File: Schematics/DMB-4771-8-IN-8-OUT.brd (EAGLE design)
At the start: 50 x 86.9 mm, 43 parts

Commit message: Modifications et ajout des cartes C
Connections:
- net S$47 renamed INT1
- net S$48 renamed SCL
- net S$49 renamed SDA
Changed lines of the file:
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@@
 <wire x1="25.4" y1="42.6275" x2="25.4" y2="36.9697" width="0.4064" layer="1"/>
 </signal>
-<signal name="S$48">
+<signal name="SCL">
 <contactref element="E$17" pad="12"/>
 <contactref element="E$60" pad="6"/>
@@
 <via x="14.2875" y="39.6875" extent="1-16" drill="0.5"/>
 </signal>
-<signal name="S$49">
+<signal name="SDA">
 <contactref element="E$60" pad="5"/>
 <contactref element="E$17" pad="13"/>
@@
 <wire x1="34.6075" y1="59.055" x2="34.6075" y2="62.3316" width="0.4064" layer="1"/>
 </signal>
-<signal name="S$47">
+<signal name="INT1">
 <contactref element="E$17" pad="20"/>
 <contactref element="E$60" pad="1"/>

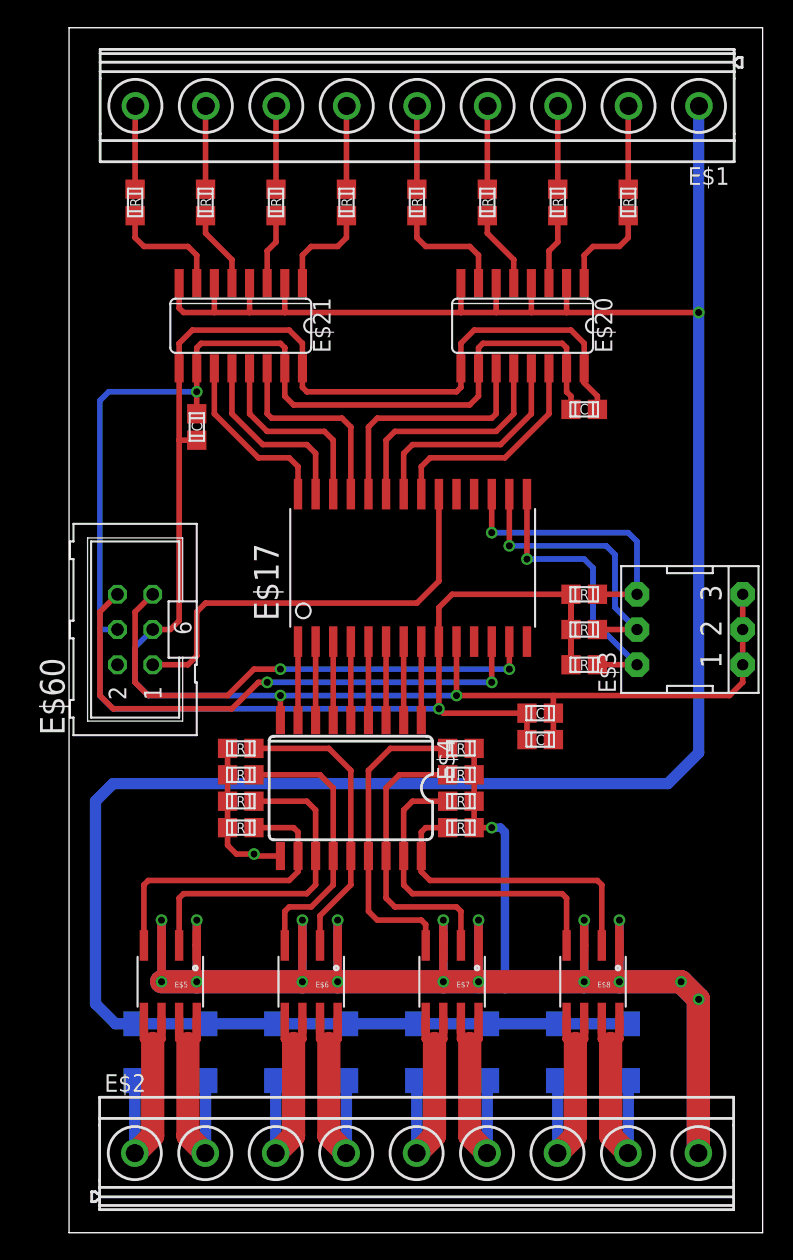
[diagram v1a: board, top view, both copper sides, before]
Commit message: Ajout cape et modification cartes C
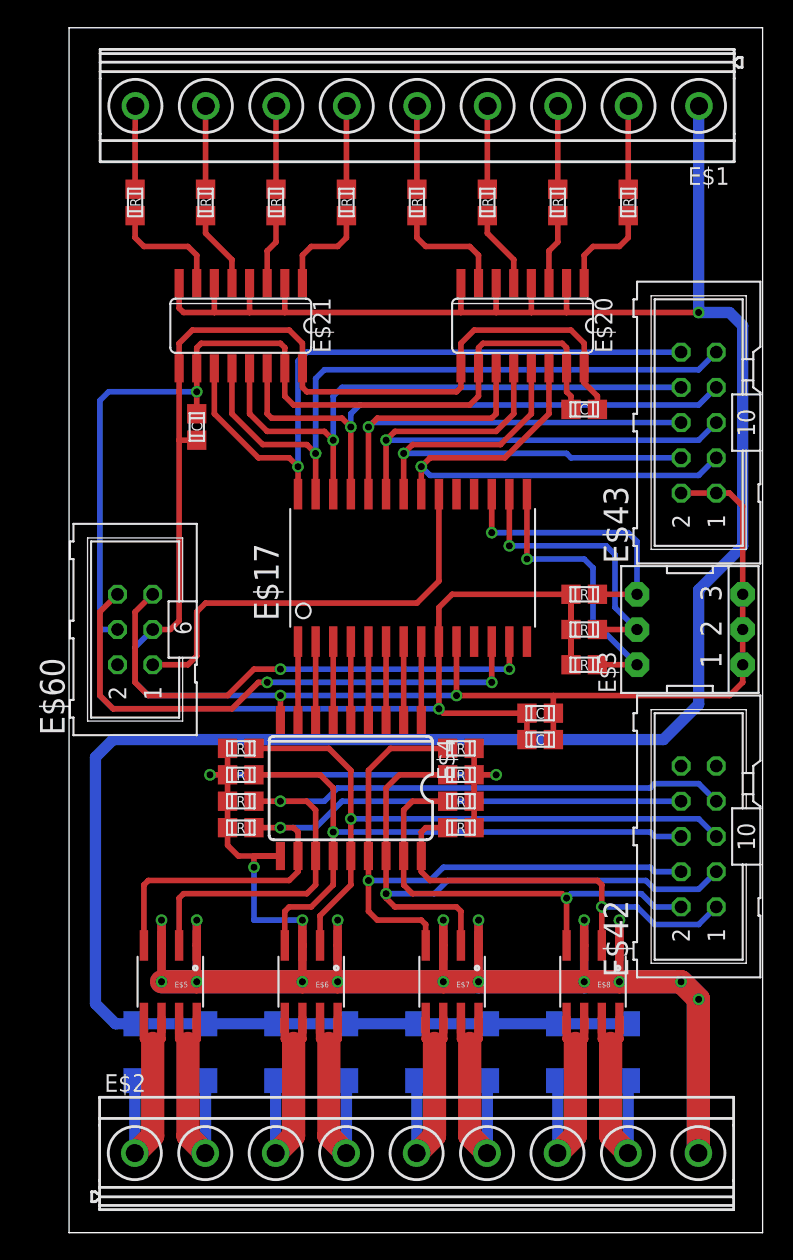
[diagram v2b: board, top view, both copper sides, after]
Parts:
- added E$42, E$43: (no value), con-harting-ml:ML10
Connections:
- removed net S$88: E$12.2, E$13.2, E$14.2, E$15.2, E$2.9, E$5.1, E$5.3, E$6.1, E$6.3, E$7.1, E$7.3, E$8.1, E$8.3
- removed net S$89: E$17.28, E$21.11
- new net S$15: E$17.28, E$21.11, E$43.10
- net GND: now also E$43.1, E$43.2
- net S$20: now also E$42.8
- net S$21: now also E$42.7
- net S$23: now also E$42.6
- net S$25: now also E$42.5
- net S$28: now also E$42.4
- net S$29: now also E$42.3
- net S$31: now also E$42.2
- net S$32: now also E$42.1
- net S$9: now also E$12.2, E$13.2, E$14.2, E$15.2, E$2.9, E$5.1, E$5.3, E$6.1, E$6.3, E$7.1, E$7.3, E$8.1, E$8.3
- net S$90: now also E$43.9
- net S$91: now also E$43.8
- net S$92: now also E$43.7
- net S$93: now also E$43.6
- net S$94: now also E$43.5
- net S$95: now also E$43.4
- net S$96: now also E$43.3
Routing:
- net S$9: track 11.1 -> 222.4 mm, vias 1 -> 20
- net S$88: track 190.9 -> 0.00 mm, vias 18 -> 0
- net S$15: track 0.00 -> 48.4 mm, vias 0 -> 1
- net S$90: track 13.4 -> 48.5 mm, vias 0 -> 1
- net S$21: track 23.8 -> 56.2 mm, vias 0 -> 1
- net S$20: track 22.0 -> 51.7 mm, vias 0 -> 1
- net S$91: track 14.0 -> 42.5 mm, vias 0 -> 1
- net S$92: track 14.5 -> 42.6 mm, vias 0 -> 1
- net S$25: track 21.2 -> 48.1 mm, vias 0 -> 1
- net S$23: track 19.8 -> 45.1 mm, vias 0 -> 1
- net S$29: track 21.0 -> 46.0 mm, vias 0 -> 1
- net S$94: track 17.2 -> 41.5 mm, vias 0 -> 1
- net S$28: track 22.6 -> 45.6 mm, vias 0 -> 1
- net S$93: track 17.7 -> 40.4 mm, vias 0 -> 1
- net S$96: track 16.0 -> 38.1 mm, vias 0 -> 1
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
